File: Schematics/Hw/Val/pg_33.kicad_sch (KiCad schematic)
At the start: 21 parts, among them U3501 F181, U3502 F181, U3503 F181, U3504 F181, U3505 F181, U3506 F181, U3507 F181, U3508 F181, U3509 F182, U3510 F182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

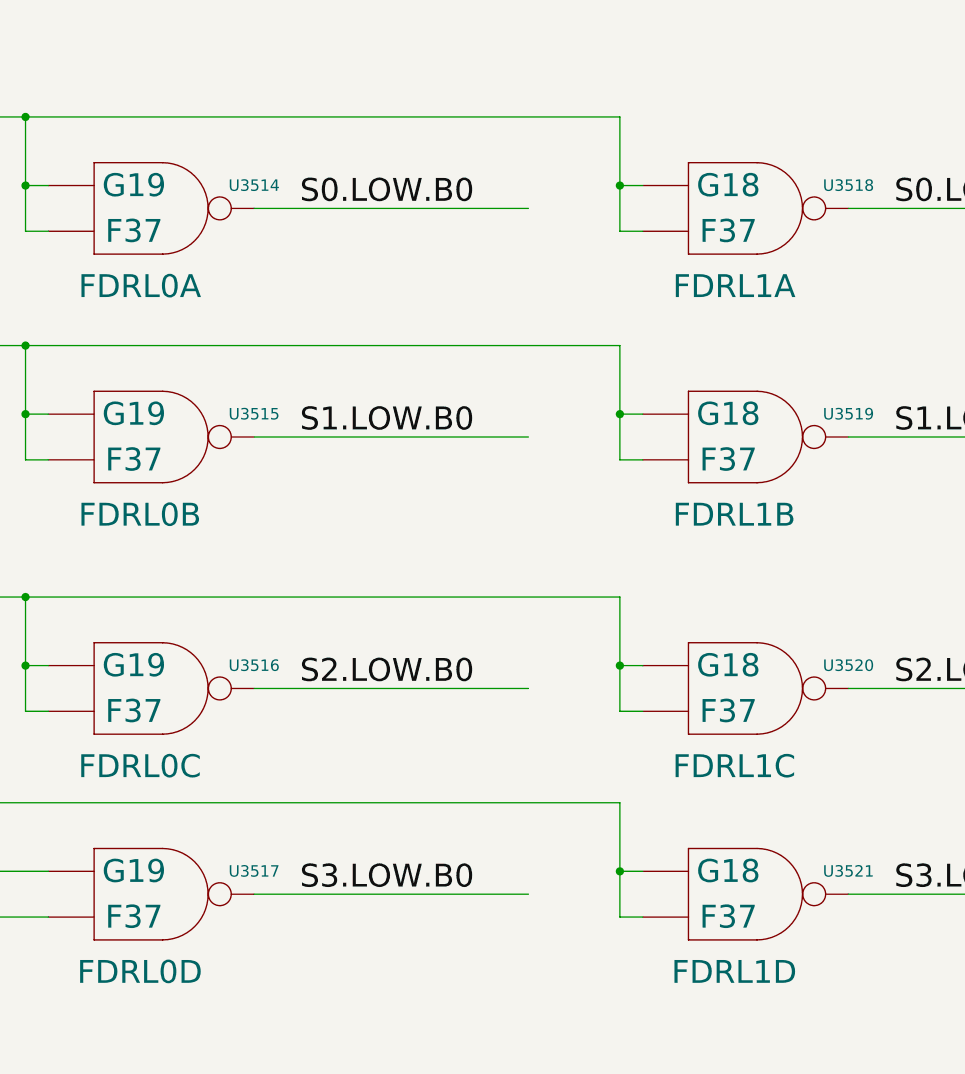
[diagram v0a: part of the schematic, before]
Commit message: Upgrade to KiCad9
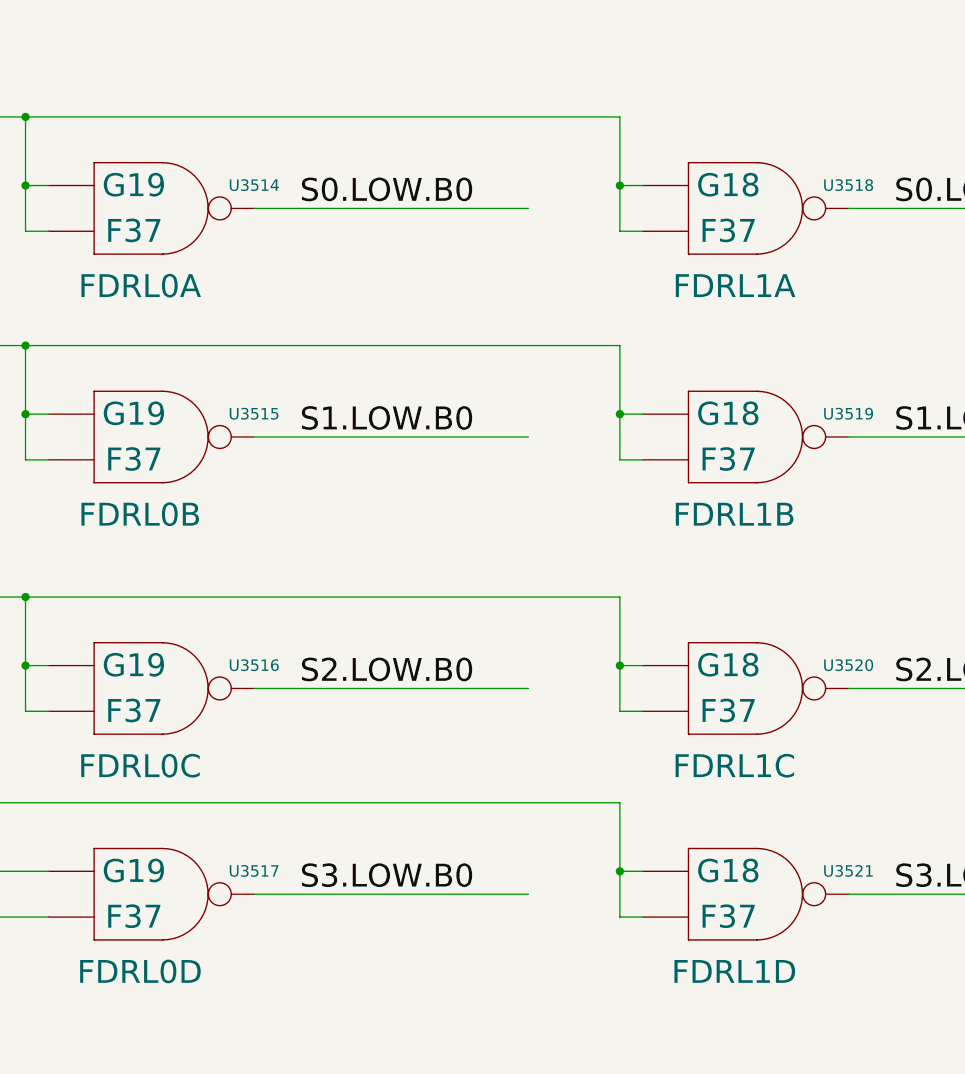
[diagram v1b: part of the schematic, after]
